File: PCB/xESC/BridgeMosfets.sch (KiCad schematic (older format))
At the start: 6 parts, among them Q1 BSC440N10NS3G, Q2 BSC440N10NS3G

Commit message: wip
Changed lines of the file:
@@
 $Descr A4 11693 8268
 encoding utf-8
-Sheet 5 6
+Sheet 6 6
 Title "xESC BLDC Controller"
 Date "2021-11-02"
@@
 AR Path="/6183112C/618D9FC1/618746CC" Ref="Q3"  Part="1"
 AR Path="/6183112C/618DC168/618746CC" Ref="Q5"  Part="1"
-F 0 "Q3" H 3704 2396 50  0000 L CNN
+F 0 "Q5" H 3704 2396 50  0000 L CNN
 F 1 "BSC440N10NS3G" H 3704 2305 50  0000 L CNN
 F 2 "Package_TO_SOT_SMD:TDSON-8-1" H 3700 2275 50  0001 L CIN
@@
 AR Path="/6183112C/618D9FC1/6187B610" Ref="Q4"  Part="1"
 AR Path="/6183112C/618DC168/6187B610" Ref="Q6"  Part="1"
-F 0 "Q4" H 3704 3496 50  0000 L CNN
+F 0 "Q6" H 3704 3496 50  0000 L CNN
 F 1 "BSC440N10NS3G" H 3704 3405 50  0000 L CNN
 F 2 "Package_TO_SOT_SMD:TDSON-8-1" H 3700 3375 50  0001 L CIN
@@
 AR Path="/6183112C/618D9FC1/619384E2" Ref="R3"  Part="1"
 AR Path="/6183112C/618DC168/619384E2" Ref="R5"  Part="1"
-F 0 "R3" V 2693 2350 50  0000 C CNN
+F 0 "R5" V 2693 2350 50  0000 C CNN
 F 1 "DNP" V 2784 2350 50  0000 C CNN
 F 2 "Resistor_SMD:R_0805_2012Metric" V 2830 2350 50  0001 C CNN
@@
 AR Path="/6183112C/618D9FC1/6193ABD6" Ref="R4"  Part="1"
 AR Path="/6183112C/618DC168/6193ABD6" Ref="R6"  Part="1"
-F 0 "R4" V 2693 3450 50  0000 C CNN
+F 0 "R6" V 2693 3450 50  0000 C CNN
 F 1 "DNP" V 2784 3450 50  0000 C CNN
 F 2 "Resistor_SMD:R_0805_2012Metric" V 2830 3450 50  0001 C CNN
@@
 AR Path="/6183112C/618D9FC1/6193ADCE" Ref="JP4"  Part="1"
 AR Path="/6183112C/618DC168/6193ADCE" Ref="JP6"  Part="1"
-F 0 "JP4" H 2900 2805 50  0000 C CNN
+F 0 "JP6" H 2900 2805 50  0000 C CNN
 F 1 "SolderJumper_2_Bridged" H 2900 2714 50  0000 C CNN
 F 2 "Jumper:SolderJumper-2_P1.3mm_Bridged_Pad1.0x1.5mm" H 2900 2600 50  0001 C CNN
@@
 AR Path="/6183112C/618D9FC1/6193C72B" Ref="JP5"  Part="1"
 AR Path="/6183112C/618DC168/6193C72B" Ref="JP7"  Part="1"
-F 0 "JP5" H 2900 3905 50  0000 C CNN
+F 0 "JP7" H 2900 3905 50  0000 C CNN
 F 1 "SolderJumper_2_Bridged" H 2900 3814 50  0000 C CNN
 F 2 "Jumper:SolderJumper-2_P1.3mm_Bridged_Pad1.0x1.5mm" H 2900 3700 50  0001 C CNN

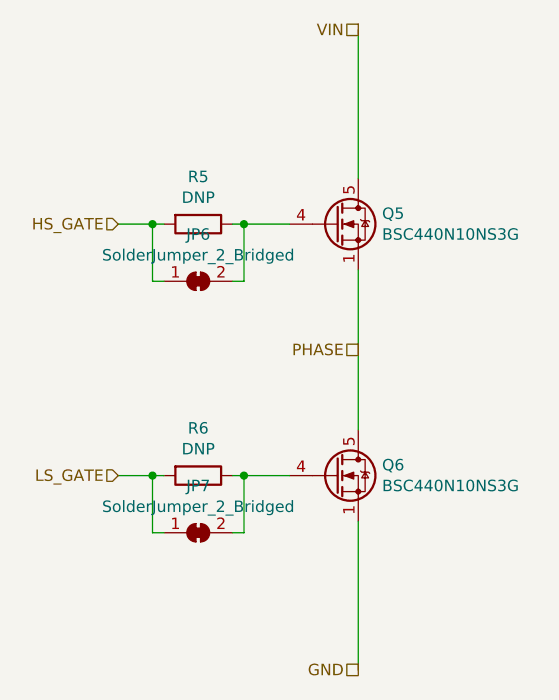
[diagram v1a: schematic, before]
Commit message: added logo, version and github link
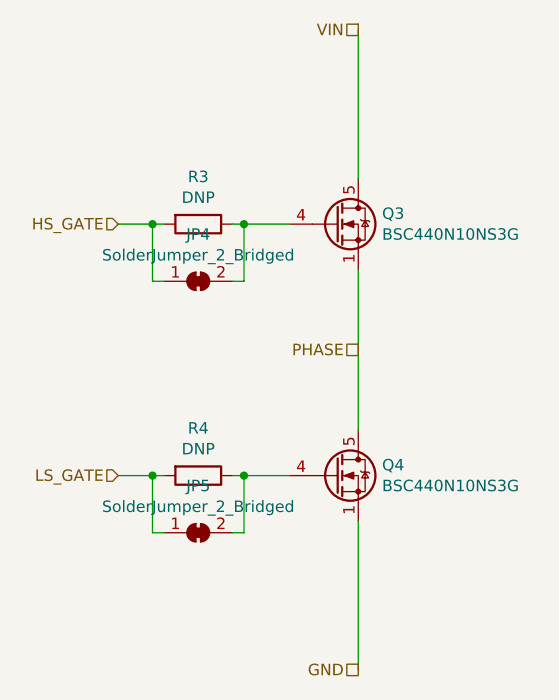
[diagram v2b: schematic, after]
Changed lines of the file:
@@
 $Descr A4 11693 8268
 encoding utf-8
-Sheet 6 6
+Sheet 5 6
 Title "xESC BLDC Controller"
 Date "2021-11-02"
@@
 AR Path="/6183112C/618D9FC1/618746CC" Ref="Q3"  Part="1"
 AR Path="/6183112C/618DC168/618746CC" Ref="Q5"  Part="1"
-F 0 "Q5" H 3704 2396 50  0000 L CNN
+F 0 "Q3" H 3704 2396 50  0000 L CNN
 F 1 "BSC440N10NS3G" H 3704 2305 50  0000 L CNN
 F 2 "Package_TO_SOT_SMD:TDSON-8-1" H 3700 2275 50  0001 L CIN
@@
 AR Path="/6183112C/618D9FC1/6187B610" Ref="Q4"  Part="1"
 AR Path="/6183112C/618DC168/6187B610" Ref="Q6"  Part="1"
-F 0 "Q6" H 3704 3496 50  0000 L CNN
+F 0 "Q4" H 3704 3496 50  0000 L CNN
 F 1 "BSC440N10NS3G" H 3704 3405 50  0000 L CNN
 F 2 "Package_TO_SOT_SMD:TDSON-8-1" H 3700 3375 50  0001 L CIN
@@
 AR Path="/6183112C/618D9FC1/619384E2" Ref="R3"  Part="1"
 AR Path="/6183112C/618DC168/619384E2" Ref="R5"  Part="1"
-F 0 "R5" V 2693 2350 50  0000 C CNN
+F 0 "R3" V 2693 2350 50  0000 C CNN
 F 1 "DNP" V 2784 2350 50  0000 C CNN
 F 2 "Resistor_SMD:R_0805_2012Metric" V 2830 2350 50  0001 C CNN
@@
 AR Path="/6183112C/618D9FC1/6193ABD6" Ref="R4"  Part="1"
 AR Path="/6183112C/618DC168/6193ABD6" Ref="R6"  Part="1"
-F 0 "R6" V 2693 3450 50  0000 C CNN
+F 0 "R4" V 2693 3450 50  0000 C CNN
 F 1 "DNP" V 2784 3450 50  0000 C CNN
 F 2 "Resistor_SMD:R_0805_2012Metric" V 2830 3450 50  0001 C CNN
@@
 AR Path="/6183112C/618D9FC1/6193ADCE" Ref="JP4"  Part="1"
 AR Path="/6183112C/618DC168/6193ADCE" Ref="JP6"  Part="1"
-F 0 "JP6" H 2900 2805 50  0000 C CNN
+F 0 "JP4" H 2900 2805 50  0000 C CNN
 F 1 "SolderJumper_2_Bridged" H 2900 2714 50  0000 C CNN
 F 2 "Jumper:SolderJumper-2_P1.3mm_Bridged_Pad1.0x1.5mm" H 2900 2600 50  0001 C CNN
@@
 AR Path="/6183112C/618D9FC1/6193C72B" Ref="JP5"  Part="1"
 AR Path="/6183112C/618DC168/6193C72B" Ref="JP7"  Part="1"
-F 0 "JP7" H 2900 3905 50  0000 C CNN
+F 0 "JP5" H 2900 3905 50  0000 C CNN
 F 1 "SolderJumper_2_Bridged" H 2900 3814 50  0000 C CNN
 F 2 "Jumper:SolderJumper-2_P1.3mm_Bridged_Pad1.0x1.5mm" H 2900 3700 50  0001 C CNN
